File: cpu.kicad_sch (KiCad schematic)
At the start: 15 parts

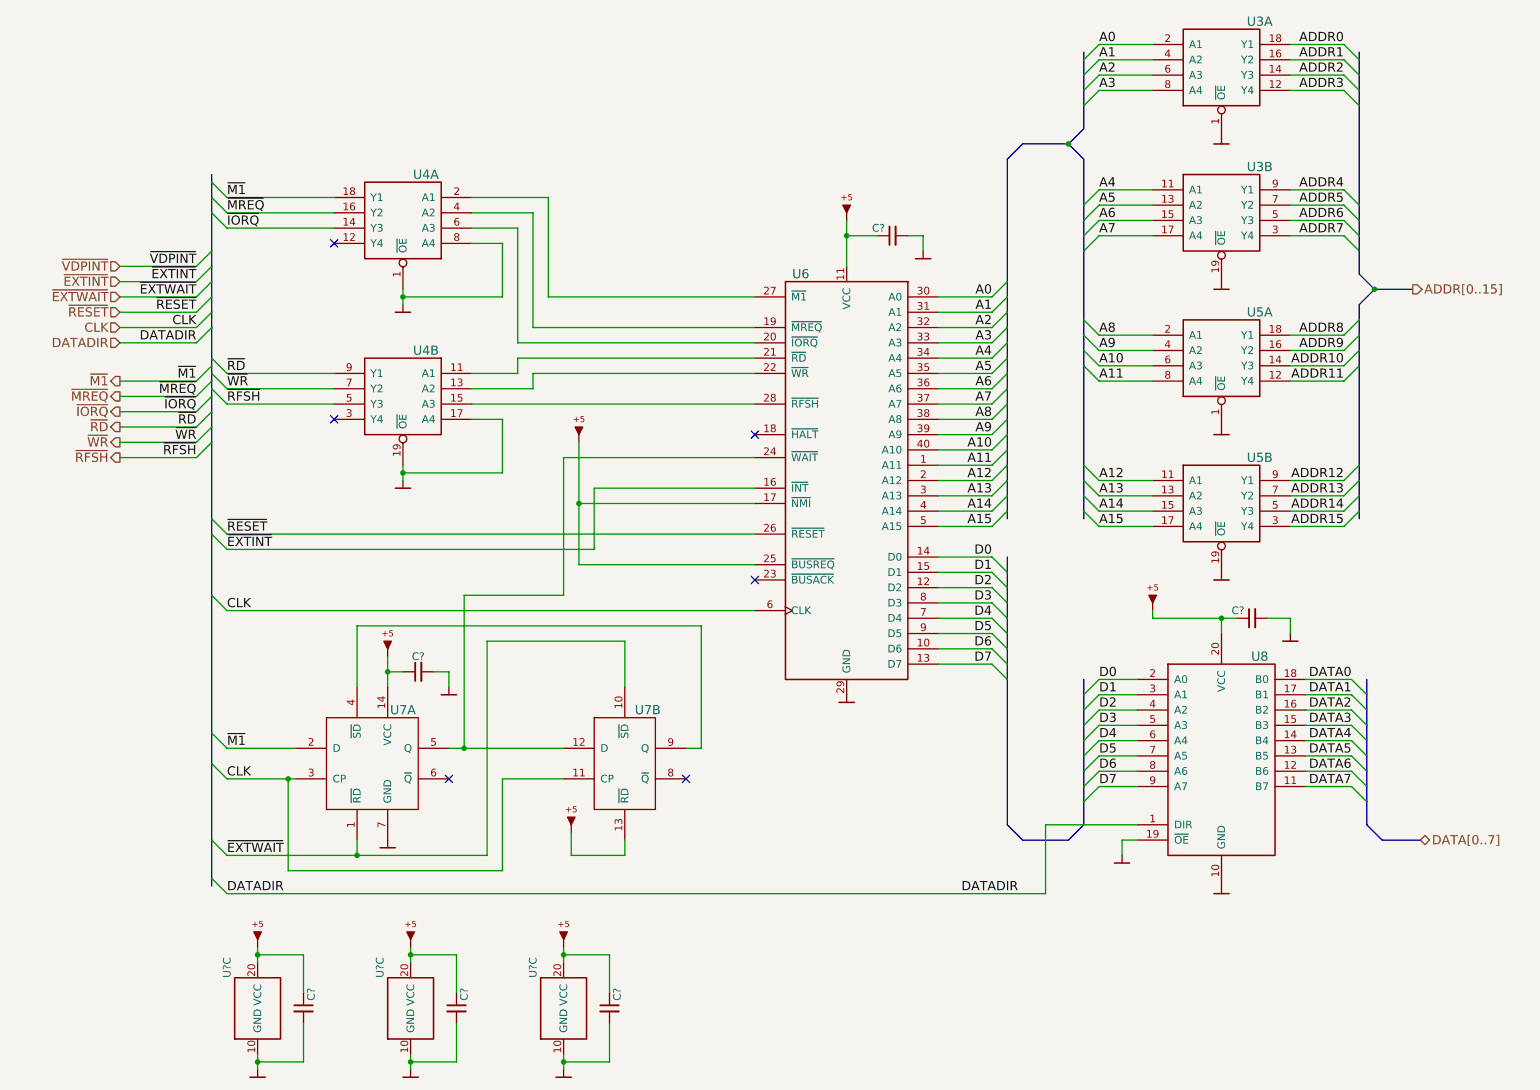
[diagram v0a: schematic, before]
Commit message: Implement power transform circuit
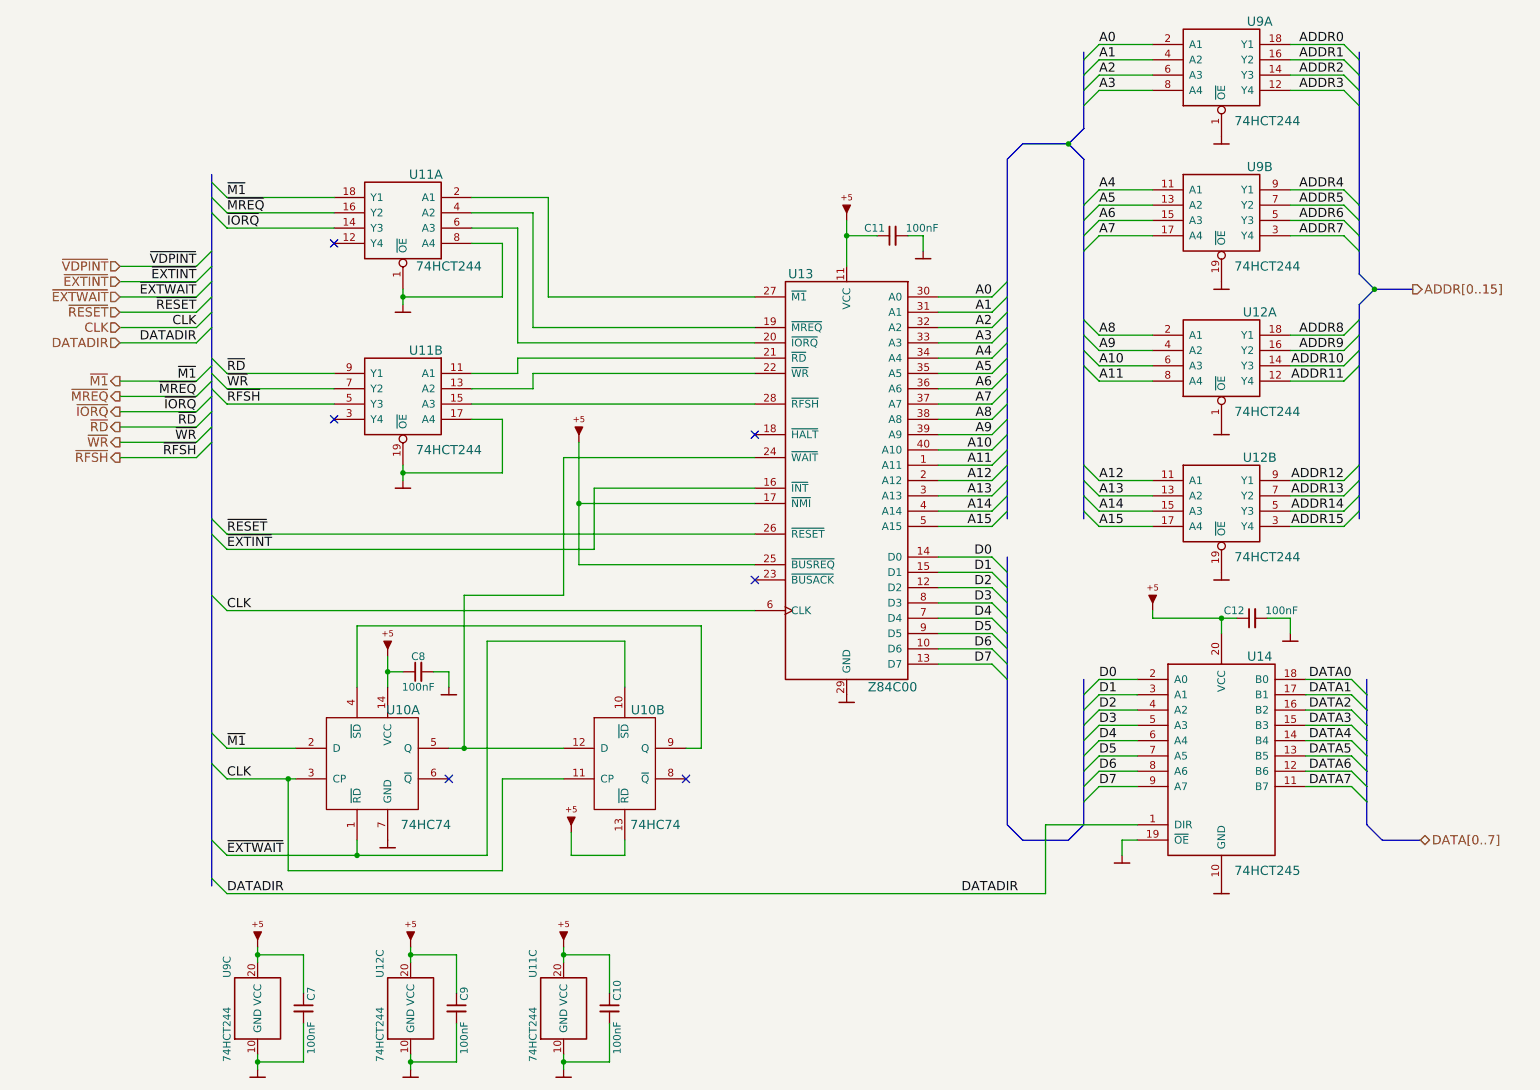
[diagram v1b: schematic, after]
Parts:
- C10, C11, C12, C7, C8, C9: renamed from C?; value (none) -> 100nF; footprint (none) -> artemisa:Disc_capacitor
- U10: renamed from U7; value (none) -> 74HC74; footprint (none) -> artemisa:DIP-14_300
- U11: renamed from U4; value (none) -> 74HCT244; footprint (none) -> artemisa:DIP-20_300
- U11, U12, U9: renamed from U?; value (none) -> 74HCT244; footprint (none) -> artemisa:DIP-20_300
- U12: renamed from U5; value (none) -> 74HCT244; footprint (none) -> artemisa:DIP-20_300
- U13: renamed from U6; value (none) -> Z84C00; footprint (none) -> artemisa:DIP-40_600
- U14: renamed from U8; value (none) -> 74HCT245; footprint (none) -> artemisa:DIP-20_300
- U9: renamed from U3; value (none) -> 74HCT244; footprint (none) -> artemisa:DIP-20_300
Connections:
- net VCC: now reaches C11.1, U13.11 (VCC)
- net VCC: now also C10.1, C12.1, C7.1, C8.1, C9.1, U10.13 (~{RD}), U10.14 (VCC), U11.20 (VCC), U12.20 (VCC), U13.17 (~{NMI}), U13.25 (~{BUSREQ}), U14.20 (VCC), U9.20 (VCC)
